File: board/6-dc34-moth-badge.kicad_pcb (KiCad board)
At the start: 2 copper layers, 75.9 x 96.4 mm, 41 parts, among them J1 USB C, J2 USB Tongue, J3 Conn_01x08, SW1 SW_SPDT, SW2 SW_SPDT, SW3 Mode SW, SW4 ATtiny battery power, U1 CH340E, U2 ATtiny814-SS, U3 AP2112K-3.3, X1 Simple_Addon_v2

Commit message: v1.0 board
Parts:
- added C3: 0.1u, Capacitor_SMD:C_1206_3216Metric_Pad1.33x1.80mm_HandSolder, B.Cu at (136.5, 130.8)
- added C4: 0.1u, Capacitor_SMD:C_1206_3216Metric_Pad1.33x1.80mm_HandSolder, B.Cu at (129.2, 125.2)
- added F1: 1A, Fuse:Fuse_1206_3216Metric_Pad1.42x1.75mm_HandSolder, B.Cu at (141.3, 115.2)
- moved D6 12.9 mm to (134.0, 111.2), turned to 0 degrees
- moved D5 6.84 mm to (147.0, 115.2), turned to 180 degrees
- moved D3 6.45 mm to (132.2, 130.8), turned to -90 degrees
- moved R2 4.75 mm to (136.0, 135.8)
- moved R4 3.63 mm to (133.9, 107.5)
- moved C1 1.78 mm to (134.1, 118.8)
- moved C2 1.78 mm to (134.1, 115.3), turned to 0 degrees
- moved U3 1.78 mm to (133.6, 123.5)
- moved R1 1.45 mm to (156.0, 138.2)
- moved D7 1.23 mm to (140.8, 110.0)
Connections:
- J2 pad 1: Net-(D5-A) -> Net-(J2-VBUS)
- U1 pad 10: unconnected-(U1-V3-Pad10) -> Net-(U1-V3)
- U1 pad 7: +5V -> /PWR select
- U2 pad 13: unconnected-(U2-PA3-Pad13) -> /GPIO 2
- U2 pad 3: unconnected-(U2-PA5-Pad3) -> /GPIO 1
- X1 pad 5: unconnected-(X1-GPIO1-Pad5) -> /GPIO 1
- X1 pad 6: unconnected-(X1-GPIO2-Pad6) -> /GPIO 2
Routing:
- net /PWR select: track 72.5 -> 110.7 mm
- net /GPIO 2: track 0.00 -> 27.4 mm
- net Net-(J2-VBUS): track 0.00 -> 24.5 mm
- net /GPIO 1: track 0.00 -> 22.8 mm
- net Net-(D5-A): track 21.3 -> 6.74 mm
- net Net-(D6-K): track 13.3 -> 25.7 mm
- net Net-(U1-V3): track 0.00 -> 10.2 mm, vias 0 -> 2
- net Net-(D3-A): track 14.8 -> 23.1 mm
- net +5V: track 72.1 -> 64.2 mm, vias 2 -> 4
- net +3.3V: track 161.1 -> 165.7 mm
- net Net-(D6-A): track 31.4 -> 27.5 mm
- net GND: track 5.13 -> 7.52 mm, vias 20 -> 27
- net Net-(J1-CC2): track 10.5 -> 8.25 mm
- net Net-(D7-A): track 15.9 -> 18.0 mm, vias 0 -> 2
- net Net-(J1-CC1): track 8.81 -> 9.81 mm
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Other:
- board text added: "800mA MAX"
- board text added: "CR2032"
- board text added: "GND +V UPDI"
- board text added: "Mode"
- board text added: "PA4"
- board text added: "PA7 PB3 PB2"
- board text added: "PB0 PA6 PB1"
- board text added: "PW"
- board text added: "R G B"
- board text added: "TX"
- board text added: "v1.0"
- board text removed: "v0.1"

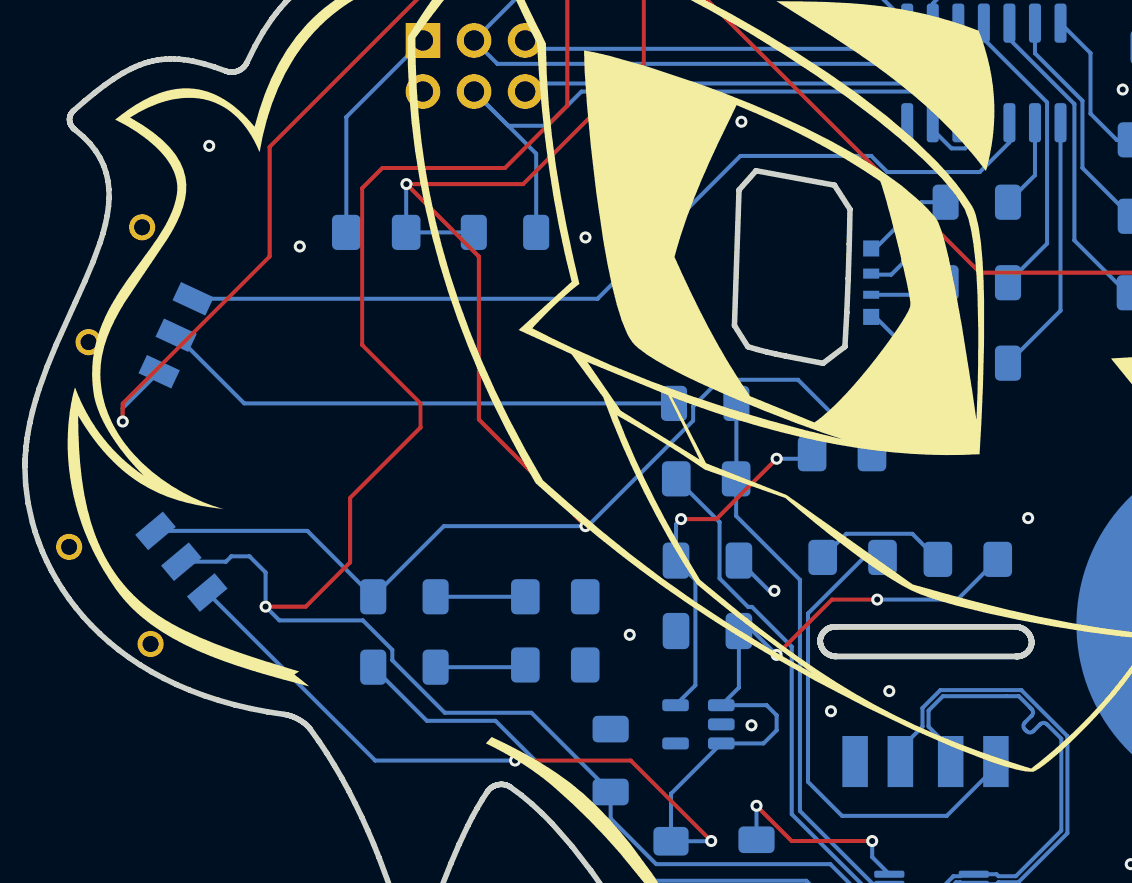
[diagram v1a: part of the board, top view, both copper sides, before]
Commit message: fix CG on switches
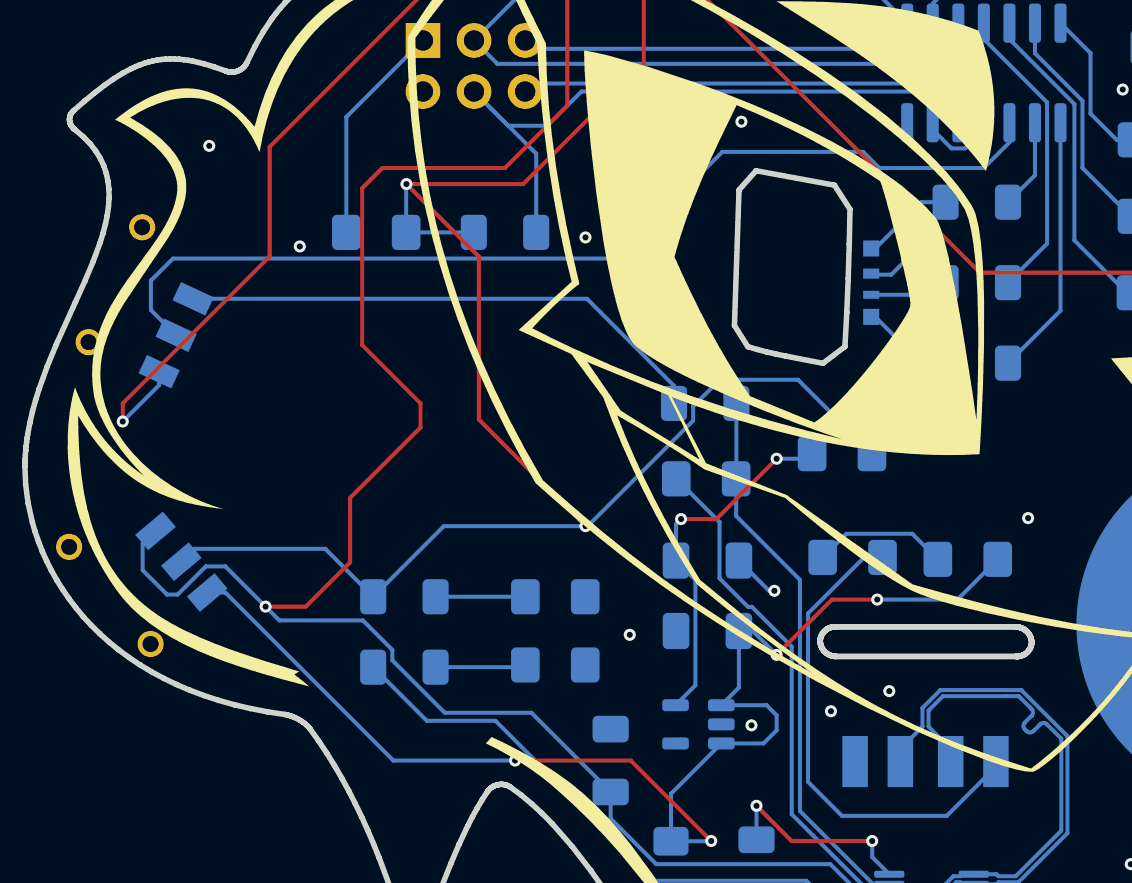
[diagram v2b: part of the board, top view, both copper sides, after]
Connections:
- SW1 pad 1: /ATtiny UPDI -> Net-(SW1-B)
- SW1 pad 2: Net-(SW1-B) -> /ATtiny UPDI
- SW2 pad 1: +3.3V -> /PWR select
- SW2 pad 2: /PWR select -> +3.3V
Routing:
- net /ATtiny UPDI: track 45.4 -> 50.4 mm
- net /PWR select: track 110.7 -> 114.6 mm
- net +3.3V: track 165.7 -> 164.3 mm
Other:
- board text added: "v1.1"
- board text removed: "v1.0"
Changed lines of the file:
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@@
 		(sheetname "/ATtiny/")
 		(sheetfile "6-dc34-moth-badge-attiny.kicad_sch")
+		(units
+			(unit
+				(name "A")
+				(pins "4" "2" "1" "3")
+			)
+		)
 		(attr smd)
 		(duplicate_pad_numbers_are_jumpers no)
@@
 			(unit
 				(name "A")
-				(pins "2" "1" "3")
+				(pins "1" "3" "2")
 			)
 		)
@@
 			(size 1 1.8)
 			(layers "B.Cu" "B.Mask" "B.Paste")
-			(net "/ATtiny UPDI")
-			(pinfunction "A_1")
+			(net "Net-(SW1-B)")
+			(pinfunction "B_1")
 			(pintype "passive")
 		)
@@
 			(size 1 1.8)
 			(layers "B.Cu" "B.Mask" "B.Paste")
-			(net "Net-(SW1-B)")
-			(pinfunction "B_2")
+			(net "/ATtiny UPDI")
+			(pinfunction "C_2")
 			(pintype "passive")
 		)
@@
 			(layers "B.Cu" "B.Mask" "B.Paste")
 			(net "/External UPDI")
-			(pinfunction "C_3")
+			(pinfunction "A_3")
 			(pintype "passive")
 		)
@@
 			(unit
 				(name "A")
-				(pins "2" "1" "3")
+				(pins "1" "3" "2")
 			)
 		)
@@
 			(size 1 1.8)
 			(layers "B.Cu" "B.Mask" "B.Paste")
-			(net "+3.3V")
-			(pinfunction "A_1")
+			(net "/PWR select")
+			(pinfunction "B_1")
 			(pintype "passive")
 		)
@@
 			(size 1 1.8)
 			(layers "B.Cu" "B.Mask" "B.Paste")
-			(net "/PWR select")
-			(pinfunction "B_2")
+			(net "+3.3V")
+			(pinfunction "C_2")
 			(pintype "passive")
 		)
@@
 			(layers "B.Cu" "B.Mask" "B.Paste")
 			(net "+5V")
-			(pinfunction "C_3")
+			(pinfunction "A_3")
 			(pintype "passive")
 		)
@@
 		(sheetname "/ATtiny/")
 		(sheetfile "6-dc34-moth-badge-attiny.kicad_sch")
+		(units
+			(unit
+				(name "A")
+				(pins "1" "2")
+			)
+		)
 		(attr smd)
 		(duplicate_pad_numbers_are_jumpers no)
@@
 		(sheetname "/ATtiny/")
 		(sheetfile "6-dc34-moth-badge-attiny.kicad_sch")
+		(units
+			(unit
+				(name "A")
+				(pins "4" "2" "1" "3")
+			)
+		)
 		(attr smd)
 		(duplicate_pad_numbers_are_jumpers no)
@@
 		(layer "Edge.Cuts")
 	)
-	(gr_text "v1.0"
+	(gr_text "v1.1"
 		(at 153.7 75.2 0)
 		(layer "B.SilkS")
@@
 			(justify left bottom mirror)
 		)
-		(render_cache "v1.0" 0
+		(render_cache "v1.1" 0
 			(polygon
 				(pts
@@
 			(polygon
 				(pts
-					(xy 150.44057 73.443822) (xy 150.513327 73.476872) (xy 150.57615 73.530353) (xy 150.601959 73.563725)
-					(xy 150.622976 73.600531) (xy 150.638554 73.639716) (xy 150.648507 73.681182) (xy 150.652398 73.728762)
-					(xy 150.652398 74.646871) (xy 150.641199 74.727283) (xy 150.607944 74.803158) (xy 150.554495 74.868349)
-					(xy 150.521668 74.89466) (xy 150.485409 74.916043) (xy 150.447413 74.931546) (xy 150.407085 74.941367)
-					(xy 150.362604 74.945) (xy 149.444862 74.945) (xy 149.367439 74.933833) (xy 149.294983 74.90076)
-					(xy 149.232131 74.847119) (xy 149.206183 74.813569) (xy 149.185015 74.776592) (xy 149.169257 74.737194)
-					(xy 149.159132 74.695554) (xy 149.155068 74.646871) (xy 149.430207 74.646871) (xy 149.439928 74.660744)
-					(xy 149.444862 74.661525) (xy 150.253336 74.661525) (xy 149.430207 73.970379) (xy 149.430207 74.646871)
-					(xy 149.155068 74.646871) (xy 149.155068 73.728762) (xy 149.157113 73.714107) (xy 149.554038 73.714107)
-					(xy 150.377259 74.405253) (xy 150.377259 73.728762) (xy 150.367628 73.714931) (xy 150.362604 73.714107)
-					(xy 149.554038 73.714107) (xy 149.157113 73.714107) (xy 149.166267 73.648509) (xy 149.199455 73.57316)
-					(xy 149.25279 73.508576) (xy 149.285613 73.482497) (xy 149.321875 73.46132) (xy 149.359999 73.445938)
-					(xy 149.400472 73.436215) (xy 149.444862 73.432648) (xy 150.362604 73.432648)
+					(xy 150.770001 73.976699) (xy 150.406659 73.976699) (xy 150.342731 73.901574) (xy 150.284843 73.833908)
+					(xy 150.284843 74.945) (xy 150.009795 74.945) (xy 150.009795 73.432648) (xy 150.314244 73.432648)
 				)
 			)
@@
 	)
 	(segment
-		(start 105 107.734758)
-		(end 106.809527 105.925231)
+		(start 106.809527 106.590473)
+		(end 105 108.4)
 		(width 0.2)
 		(layer "B.Cu")
@@
 	)
 	(segment
-		(start 105 108.4)
-		(end 105 107.734758)
+		(start 106.809527 105.925231)
+		(end 106.809527 106.590473)
 		(width 0.2)
 		(layer "B.Cu")
@@
 	)
 	(segment
-		(start 110.4 115.1)
-		(end 110.132089 115.367911)
+		(start 105.990022 114.474649)
+		(end 105.990022 115.790022)
 		(width 0.2)
 		(layer "B.Cu")
@@
 	)
 	(segment
-		(start 111.3 115.1)
-		(end 110.4 115.1)
+		(start 109.130194 115.6)
+		(end 110.1 115.6)
 		(width 0.2)
 		(layer "B.Cu")
@@
 	)
 	(segment
+		(start 107.2 117)
+		(end 107.730194 117)
+		(width 0.2)
+		(layer "B.Cu")
+		(net "/PWR select")
+	)
+	(segment
 		(start 129.25 126.8125)
 		(end 129.25 128.134744)
@@
 	)
 	(segment
+		(start 105.990022 115.790022)
+		(end 107.2 117)
+		(width 0.2)
+		(layer "B.Cu")
+		(net "/PWR select")
+	)
+	(segment
 		(start 129.25 128.134744)
 		(end 131.515256 130.4)
@@
 	)
 	(segment
-		(start 125.3125 122.875)
-		(end 121.005256 122.875)
+		(start 106.628849 113.835822)
+		(end 105.990022 114.474649)
 		(width 0.2)
 		(layer "B.Cu")
@@
 	)
 	(segment
-		(start 110.132089 115.367911)
-		(end 107.914425 115.367911)
+		(start 125.3125 122.875)
+		(end 121.005256 122.875)
 		(width 0.2)
 		(layer "B.Cu")
@@
 	)
 	(segment
-		(start 112.1 117.6)
-		(end 112.1 115.9)
+		(start 107.730194 117)
+		(end 109.130194 115.6)
 		(width 0.2)
 		(layer "B.Cu")
@@
 	)
 	(segment
-		(start 112.1 115.9)
-		(end 111.3 115.1)
+		(start 110.1 115.6)
+		(end 112.1 117.6)
 		(width 0.2)
 		(layer "B.Cu")
@@
 	)
 	(segment
-		(start 117.45 117.11)
-		(end 114.175822 113.835822)
+		(start 107.914425 115.367911)
+		(end 108.553252 114.729084)
 		(width 0.2)
 		(layer "B.Cu")
@@
 	)
 	(segment
+		(start 115.069084 114.729084)
+		(end 117.45 117.11)
+		(width 0.2)
+		(layer "B.Cu")
+		(net "+3.3V")
+	)
+	(segment
 		(start 142.2375 110)
 		(end 138.5625 106.325)
@@
 	)
 	(segment
-		(start 114.175822 113.835822)
-		(end 106.628849 113.835822)
-		(width 0.2)
-		(layer "B.Cu")
-		(net "+3.3V")
-	)
-	(segment
 		(start 159.190256 101)
 		(end 160.1 101)
@@
 	)
 	(segment
+		(start 108.553252 114.729084)
+		(end 115.069084 114.729084)
+		(width 0.2)
+		(layer "B.Cu")
+		(net "+3.3V")
+	)
+	(segment
 		(start 120.96 113.6)
 		(end 128 113.6)
@@
 	)
 	(segment
-		(start 108.5 102.3)
-		(end 128.6 102.3)
+		(start 147.794999 95.8)
+		(end 149.07 94.524999)
 		(width 0.2)
 		(layer "B.Cu")
@@
 	)
 	(segment
-		(start 149.07 94.53)
+		(start 129.5 100.3)
+		(end 134.8 95)
+		(width 0.2)
+		(layer "B.Cu")
+		(net "/ATtiny UPDI")
+	)
+	(segment
+		(start 149.07 94.524999)
 		(end 149.07 93.55)
 		(width 0.2)
@@
 	)
 	(segment
-		(start 147.6 96)
-		(end 149.07 94.53)
+		(start 134.8 95)
+		(end 141.8 95)
 		(width 0.2)
 		(layer "B.Cu")
@@
 	)
 	(segment
-		(start 143 96)
-		(end 147.6 96)
+		(start 107.654763 104.112617)
+		(end 106.4 102.857854)
 		(width 0.2)
 		(layer "B.Cu")
@@
 	)
 	(segment
-		(start 135.7 95.2)
-		(end 142.2 95.2)
+		(start 142.6 95.8)
+		(end 147.794999 95.8)
 		(width 0.2)
 		(layer "B.Cu")
@@
 	)
 	(segment
-		(start 128.6 102.3)
-		(end 135.7 95.2)
+		(start 107.5 100.3)
+		(end 129.5 100.3)
 		(width 0.2)
 		(layer "B.Cu")
@@
 	)
 	(segment
-		(start 142.2 95.2)
-		(end 143 96)
+		(start 106.4 102.857854)
+		(end 106.4 101.4)
+		(width 0.2)
+		(layer "B.Cu")
+		(net "/ATtiny UPDI")
+	)
+	(segment
+		(start 141.8 95)
+		(end 142.6 95.8)
+		(width 0.2)
+		(layer "B.Cu")
+		(net "/ATtiny UPDI")
+	)
+	(segment
+		(start 106.4 101.4)
+		(end 107.5 100.3)
 		(width 0.2)
 		(layer "B.Cu")
@@
 	)
 	(segment
-		(start 117.55 125.25)
+		(start 118.45 125.25)
 		(end 124.5 125.25)
 		(width 0.2)
@@
 	)
 	(segment
+		(start 135.625 121.625)
+		(end 134.75 122.5)
+		(width 0.2)
+		(layer "B.Cu")
+		(net "+5V")
+	)
+	(segment
 		(start 109.2 116.9)
-		(end 117.55 125.25)
+		(end 110.1 116.9)
 		(width 0.2)
 		(layer "B.Cu")
@@
 	)
 	(segment
-		(start 135.625 121.625)
-		(end 134.75 122.5)
+		(start 110.1 116.9)
+		(end 118.45 125.25)
 		(width 0.2)
 		(layer "B.Cu")
@@
 	)
 	(segment
-		(start 111.042146 107.5)
-		(end 107.654763 104.112617)
+		(start 128.075 102.3)
+		(end 132.4 106.625)
+		(width 0.2)
+		(layer "B.Cu")
+		(net "Net-(SW1-B)")
+	)
+	(segment
+		(start 108.5 102.3)
+		(end 128.075 102.3)
 		(width 0.2)
 		(layer "B.Cu")
@@
 	)
 	(segment
-		(start 132.4 107.5)
-		(end 111.042146 107.5)
+		(start 132.4 106.625)
+		(end 132.4 107.5)
 		(width 0.2)
 		(layer "B.Cu")
